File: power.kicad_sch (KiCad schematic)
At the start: 44 parts, among them IC1 MP9943AGQ-Z, IC2 MP9943AGQ-Z, U4 AP2112K-3.3TRG1, U5 AP2112K-1.8TRG1

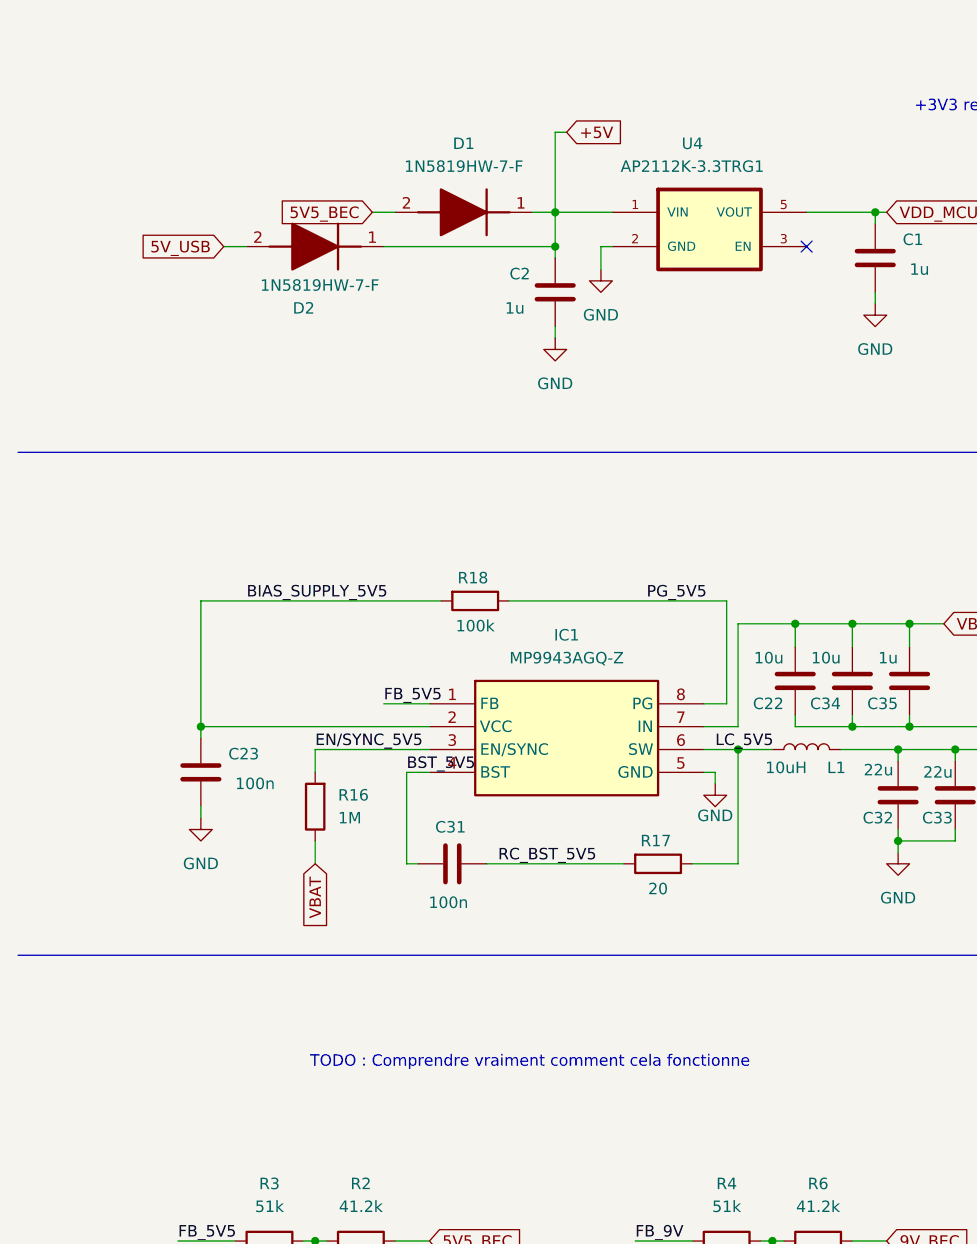
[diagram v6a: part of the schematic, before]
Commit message: removed schottky diodes to use ideal diodes smaller
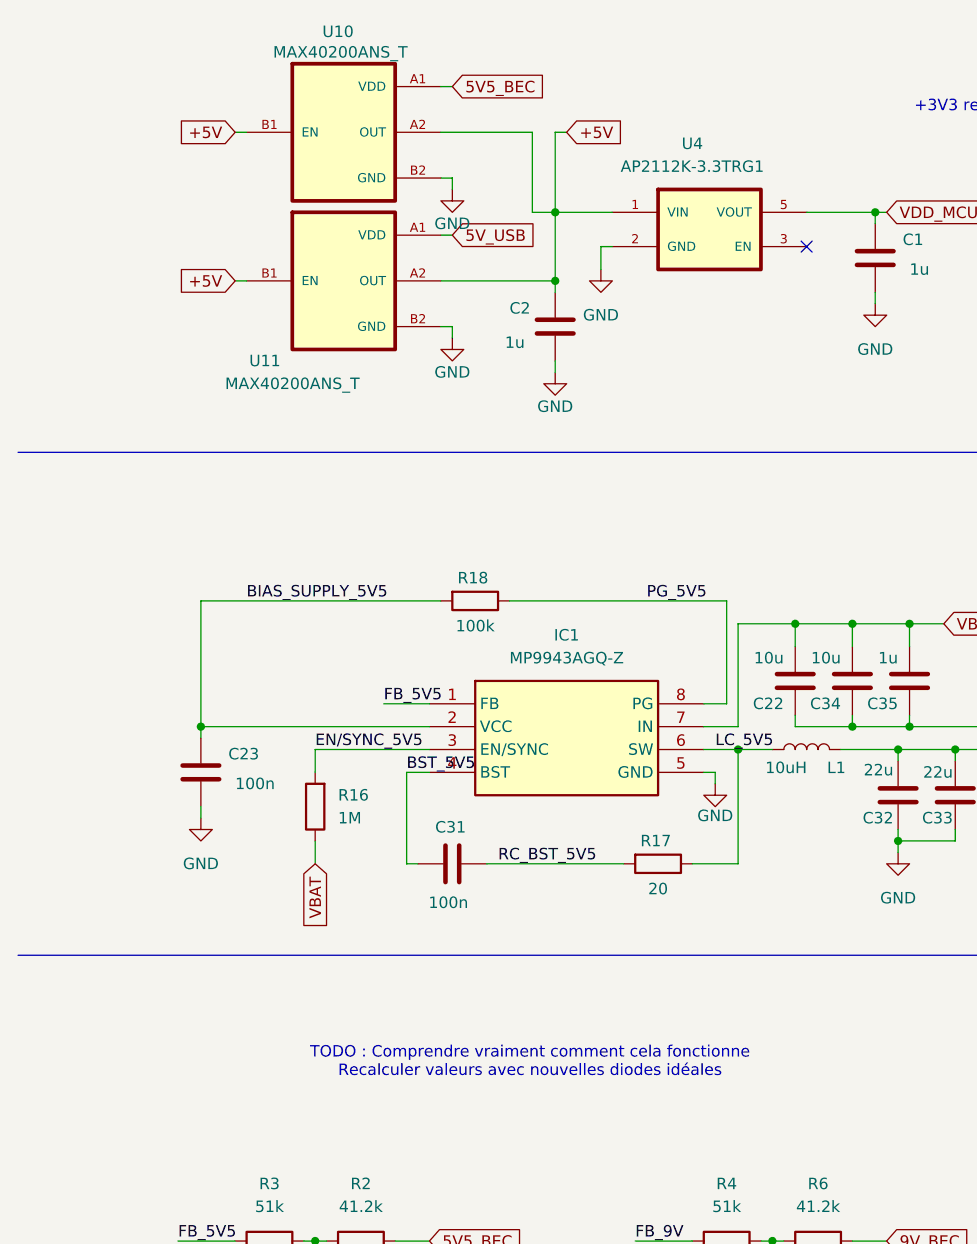
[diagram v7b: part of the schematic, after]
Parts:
- removed D1, D2: 1N5819HW-7-F, fcg4_fp:SOD3716X145M, symbol fcg4:1N5819HW-7-F
- added U10, U11: MAX40200ANS_T, fcg4_fp:BGA4N35P2X2_72X72X50N, symbol fcg4:MAX40200ANS_T
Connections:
- net +5V: now also U10.A2 (OUT), U10.B1 (EN), U11.A2 (OUT), U11.B1 (EN)
- net 5V5_BEC: now also U10.A1 (VDD)
- net 5V_USB: now also U11.A1 (VDD)
- net GND: now also U10.B2 (GND), U11.B2 (GND)
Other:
- note added: "TODO : Comprendre vraiment comment cela fonctionne Recalculer valeurs avec nouvelles diodes idéales"
- note removed: "TODO : Comprendre vraiment comment cela fonctionne"
- moved on the sheet: C2

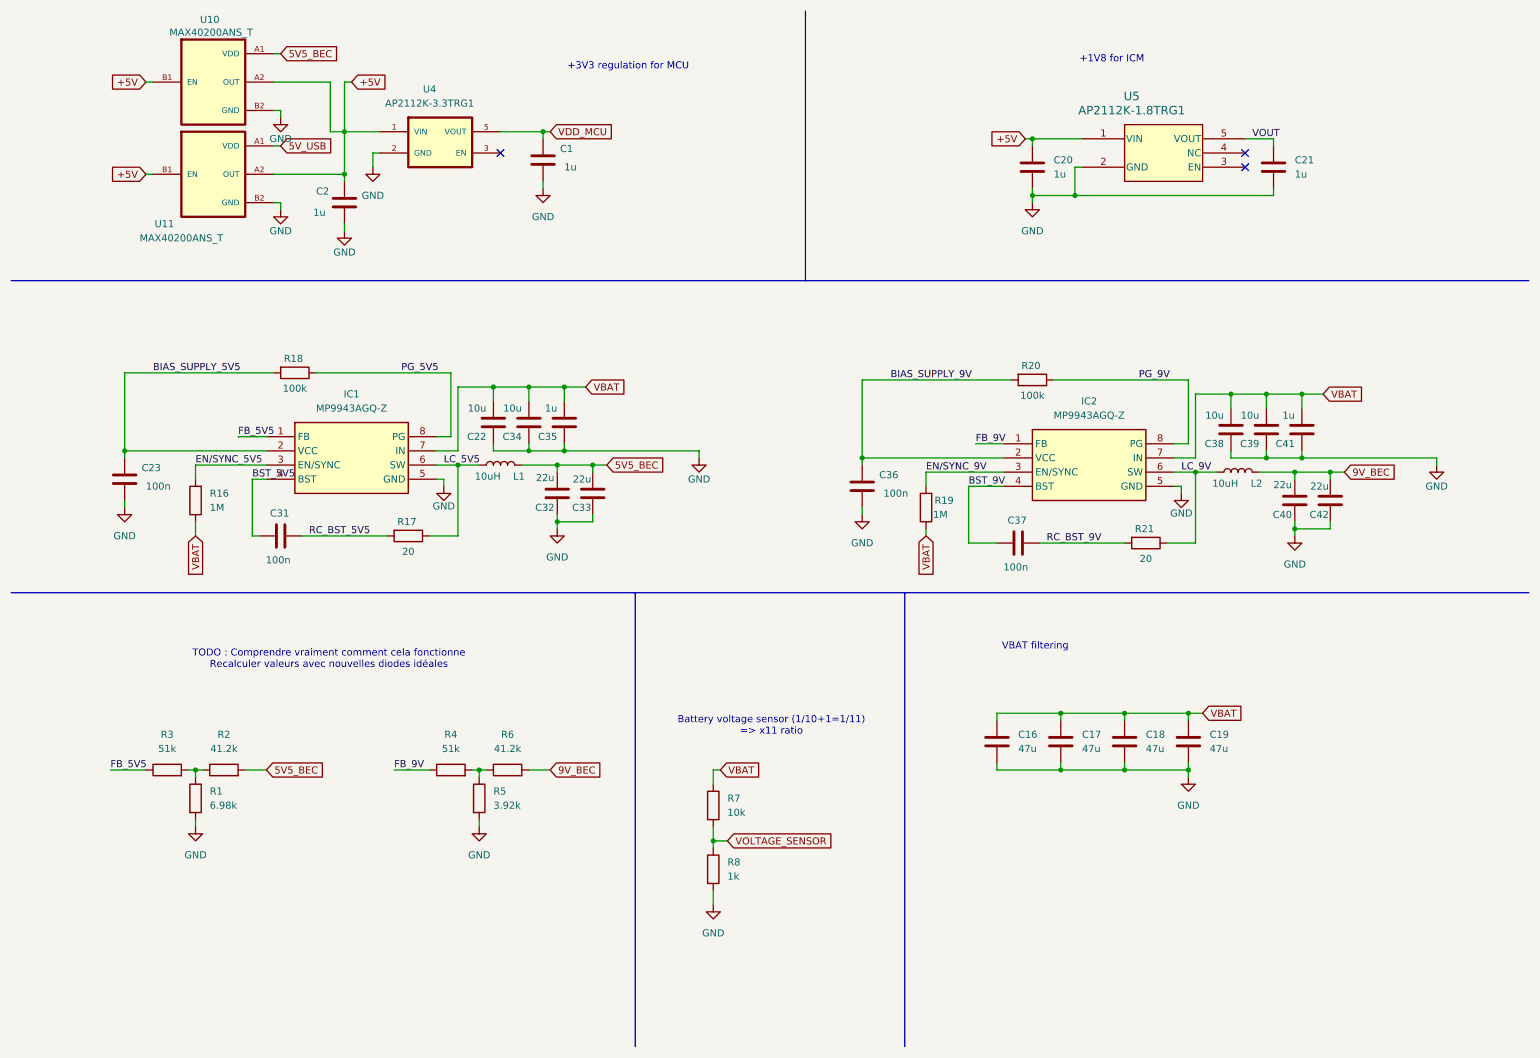
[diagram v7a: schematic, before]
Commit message: add 100ohm for pwm and some routing
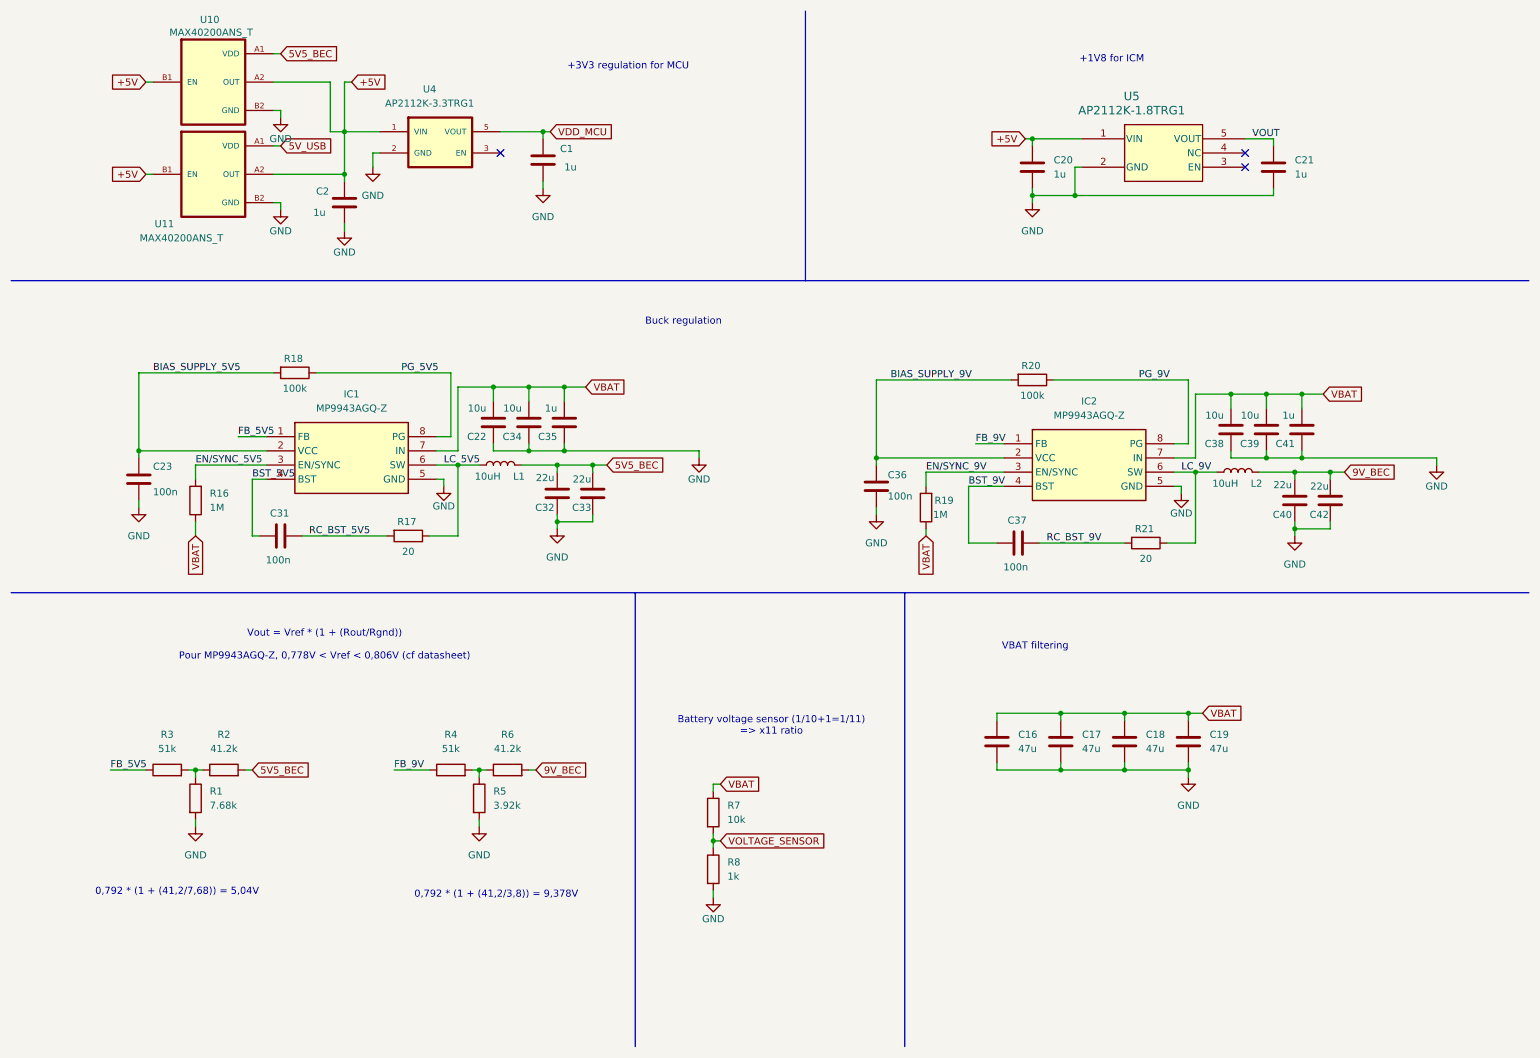
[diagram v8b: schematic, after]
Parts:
- R1: value 6.98k -> 7.68k
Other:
- note added: "0,792 * (1 + (41,2/3,8)) = 9,378V"
- note added: "0,792 * (1 + (41,2/7,68)) = 5,04V"
- note added: "Buck regulation"
- note added: "Vout = Vref * (1 + (Rout/Rgnd)) Pour MP9943AGQ-Z, 0,778V < Vref < 0,806V (cf datasheet)"
- note removed: "TODO : Comprendre vraiment comment cela fonctionne Recalculer valeurs avec nouvelles diodes idéales"
- moved on the sheet: C23, C36, R7
